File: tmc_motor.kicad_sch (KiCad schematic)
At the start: 10 parts

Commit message: starting layout
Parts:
- R202: renamed from R; footprint Resistor_SMD:R_0805_2012Metric_Pad1.20x1.40mm_HandSolder -> Resistor_SMD:R_0603_1608Metric_Pad0.98x0.95mm_HandSolder
- R203, R205: footprint Resistor_SMD:R_0805_2012Metric_Pad1.20x1.40mm_HandSolder -> Resistor_SMD:R_0603_1608Metric_Pad0.98x0.95mm_HandSolder
- SW201: renamed from SW; footprint (none) -> Button_Switch_THT:SW_DIP_SPSTx02_Slide_9.78x7.26mm_W7.62mm_P2.54mm
- renumbered C to C202, J to J201, U to U201

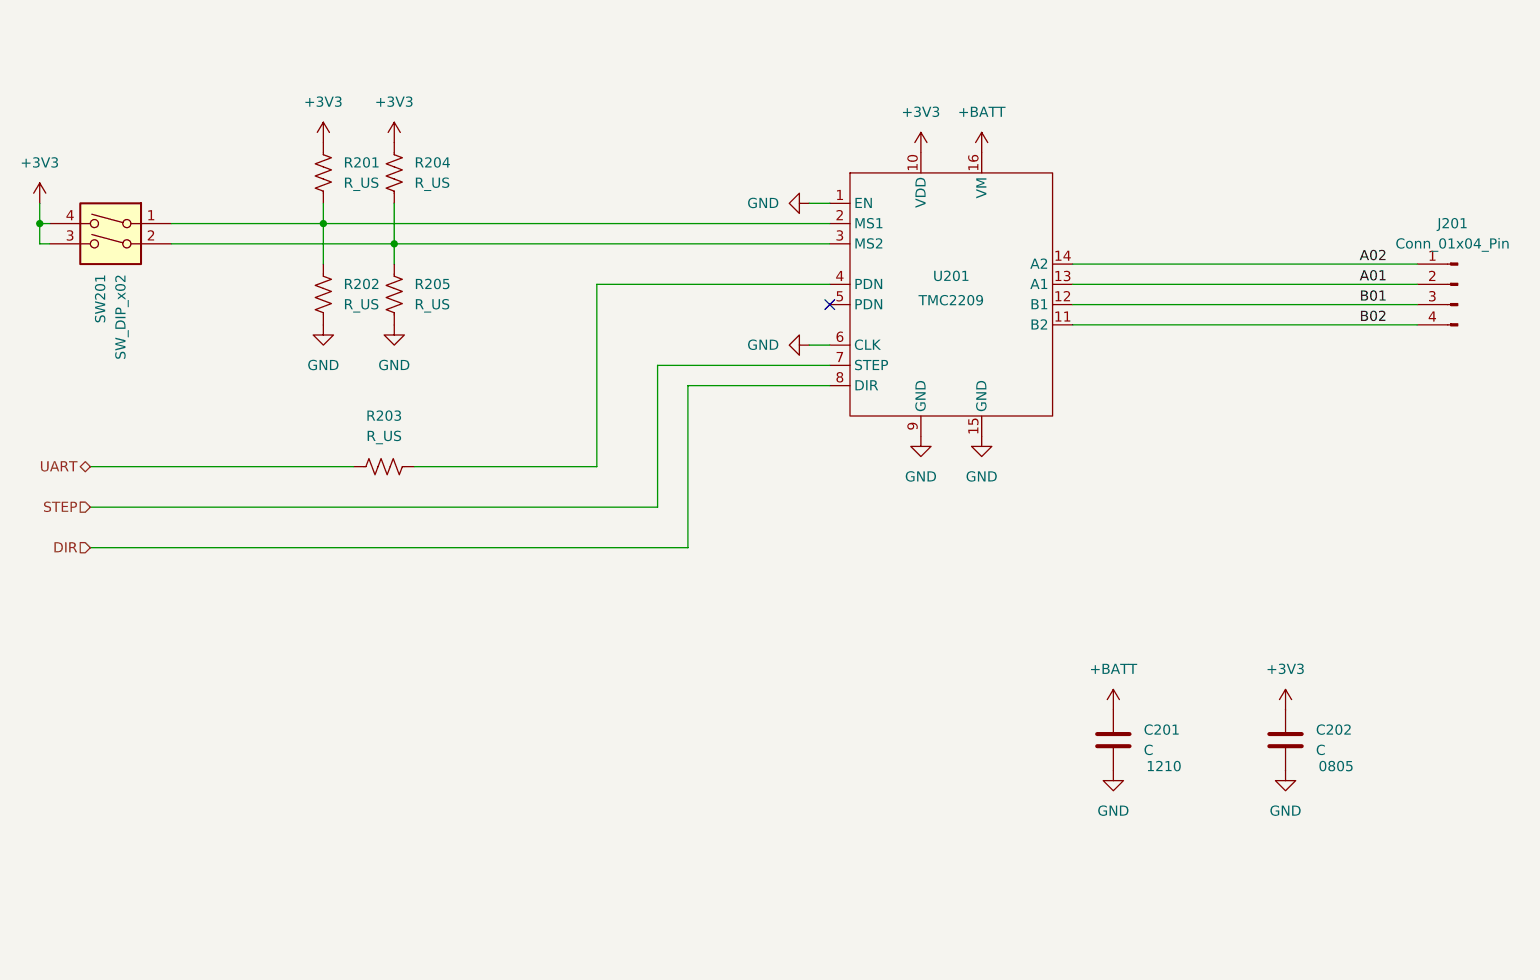
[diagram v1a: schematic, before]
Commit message: Add net class
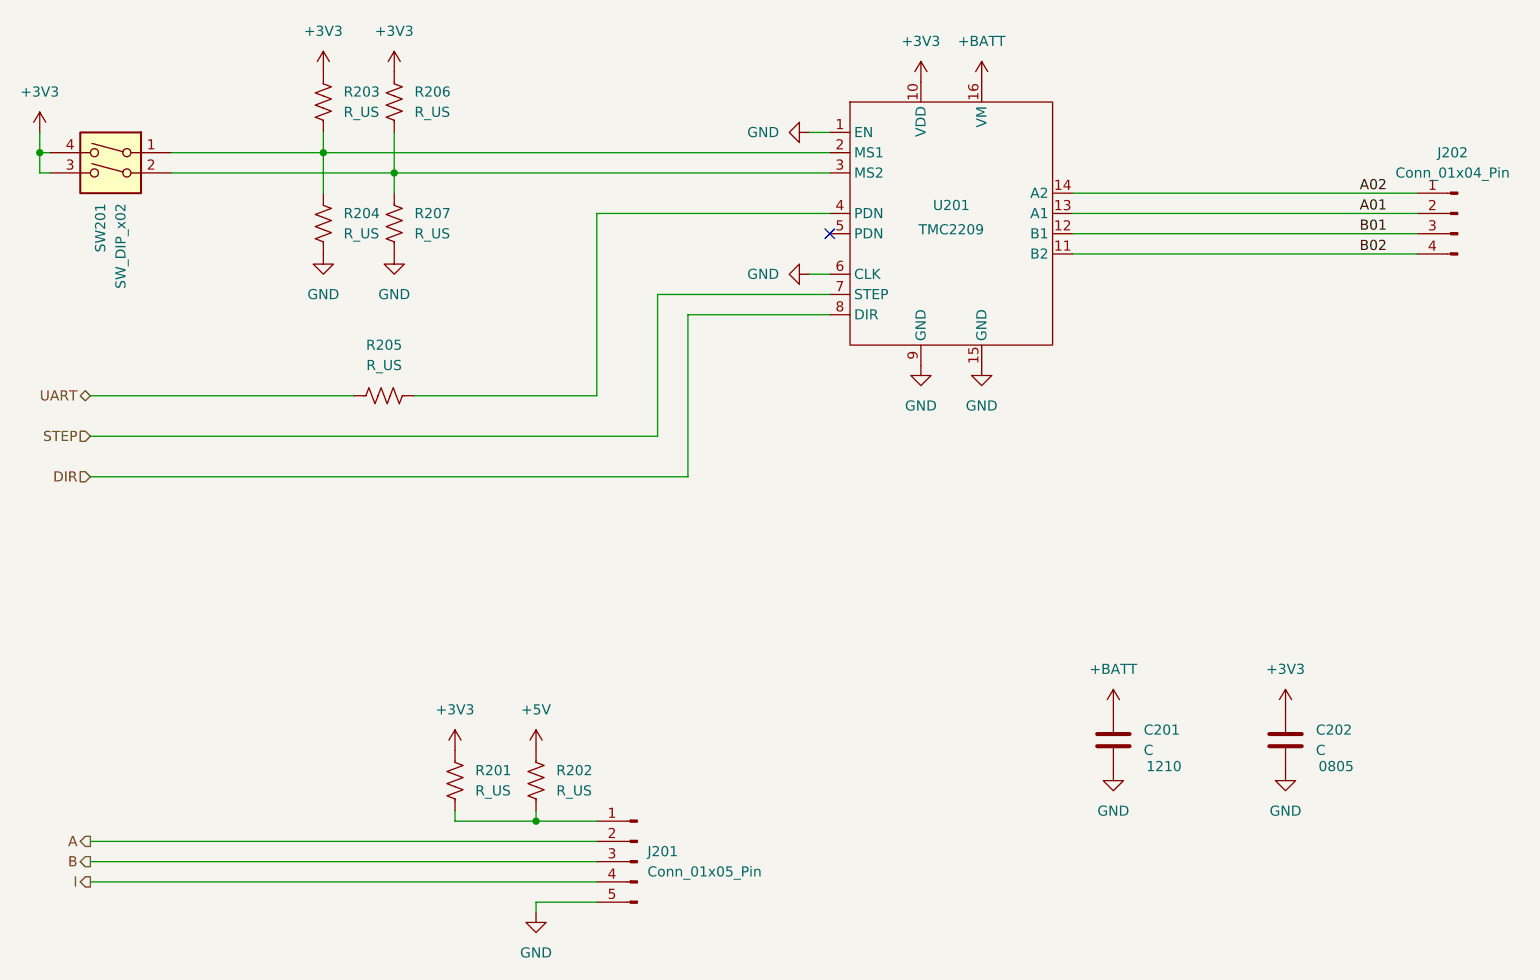
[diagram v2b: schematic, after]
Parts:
- added J201: Conn_01x05_Pin, Connector_Molex:Molex_KK-254_AE-6410-05A_1x05_P2.54mm_Vertical, symbol Connector:Conn_01x05_Pin
- added R201, R202: R_US, Resistor_SMD:R_0603_1608Metric_Pad0.98x0.95mm_HandSolder, symbol Device:R_US
- renumbered J201 to J202, R201 to R203, R202 to R204, R203 to R205, R204 to R206, R205 to R207
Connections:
- net +3V3: now also R201.2
- net GND: now also J201.5 (Pin_5)
- new net: J201.1 (Pin_1), R201.1, R202.1
- new net +5V: R202.2
- new net A: J201.2 (Pin_2)
- new net B: J201.3 (Pin_3)
- new net I: J201.4 (Pin_4)
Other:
- moved on the sheet: J202, R203, R204, R205, R206, R207, SW201, U201

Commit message: move encoder pull up resistor to tmc sheet
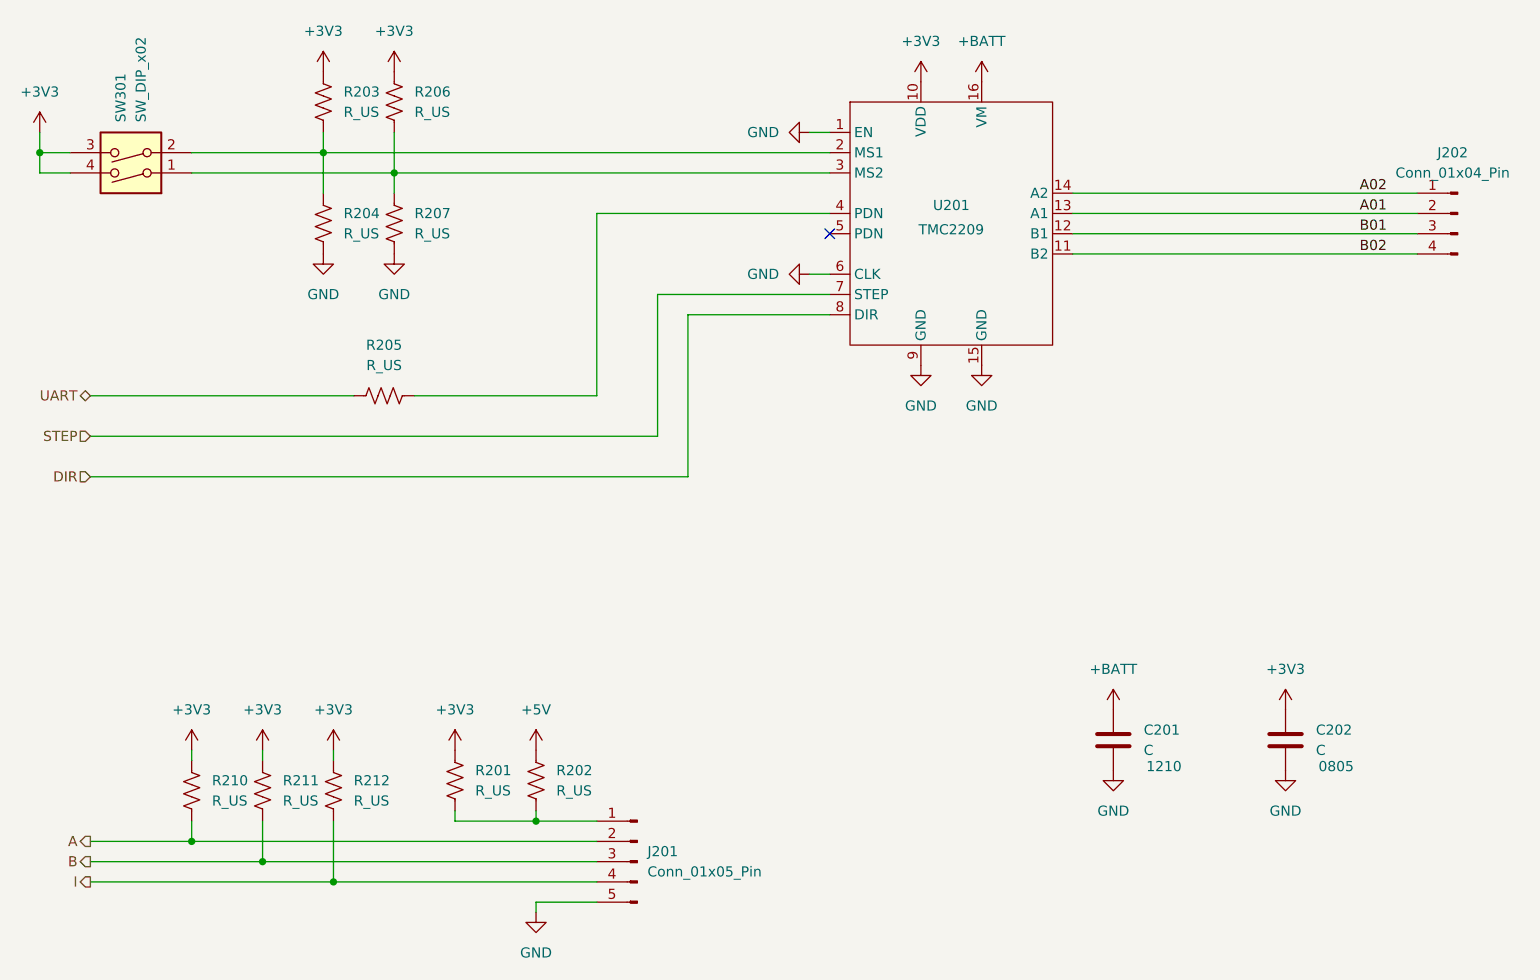
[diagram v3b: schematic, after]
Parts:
- added R210, R211, R212: R_US, Resistor_SMD:R_0603_1608Metric_Pad0.98x0.95mm_HandSolder, symbol Device:R_US
- renumbered SW201 to SW301
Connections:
- net +3V3: now also R210.2, R211.2, R212.2
- net A: now also R210.1
- net B: now also R211.1
- net I: now also R212.1
- net at R206.2, R207.1, U201.3 (MS2): now also SW301.1; no longer SW301.2
- net at R203.2, R204.1, U201.2 (MS1): now also SW301.2; no longer SW301.1
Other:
- moved on the sheet: SW301

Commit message: hrtim
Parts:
- removed R205: R_US, Resistor_SMD:R_0603_1608Metric_Pad0.98x0.95mm_HandSolder, symbol Device:R_US
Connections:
- net UART: now also U201.4 (PDN)
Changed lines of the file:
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@@
 	(wire
 		(pts
-			(xy 57.15 102.87) (xy 90.17 102.87)
+			(xy 57.15 102.87) (xy 120.65 102.87)
 		)
 		(stroke
@@
 		(pts
 			(xy 69.85 158.75) (xy 120.65 158.75)
-		)
-		(stroke
-			(width 0)
-			(type default)
-		)
-	)
-	(wire
-		(pts
-			(xy 97.79 102.87) (xy 120.65 102.87)
 		)
 		(stroke
@@
 					(unit 1)
 				)
-			)
-		)
-	)
-	(symbol
-		(lib_id "Device:R_US")
-		(at 93.98 102.87 90)
-		(unit 1)
-		(exclude_from_sim no)
-		(in_bom yes)
-		(on_board yes)
-		(dnp no)
-		(fields_autoplaced yes)
-		(property "Reference" "R205"
-			(at 93.98 96.52 90)
-			(effects
-				(font
-					(size 1.27 1.27)
-				)
-			)
-		)
-		(property "Value" "R_US"
-			(at 93.98 99.06 90)
-			(effects
-				(font
-					(size 1.27 1.27)
-				)
-			)
-		)
-		(property "Footprint" "Resistor_SMD:R_0603_1608Metric_Pad0.98x0.95mm_HandSolder"
-			(at 94.234 101.854 90)
-			(effects
-				(font
-					(size 1.27 1.27)
-				)
-				(hide yes)
-			)
-		)
-		(property "Datasheet" "~"
-			(at 93.98 102.87 0)
-			(effects
-				(font
-					(size 1.27 1.27)
-				)
-				(hide yes)
-			)
-		)
-		(property "Description" "Resistor, US symbol"
-			(at 93.98 102.87 0)
-			(effects
-				(font
-					(size 1.27 1.27)
-				)
-				(hide yes)
-			)
-		)
-		(pin "1"
-		)
-		(pin "2"
-		)
-		(instances
-			(project "Carte_moteur"
-				(path "/5d858058-eb89-4613-a7ba-0652b9f0936c/3601c837-7861-4e39-9e5f-37bf5bd7778d"
-					(reference "R205")
-					(unit 1)
-				)
-				(path "/5d858058-eb89-4613-a7ba-0652b9f0936c/37d501de-32d1-405a-b67e-90954dd4eb6d"
-					(reference "R405")
-					(unit 1)
-				)
-				(path "/5d858058-eb89-4613-a7ba-0652b9f0936c/775cd45e-9174-4367-b4d9-b516ea5d1b35"
-					(reference "R305")
-					(unit 1)
-				)

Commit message: before trying new µC orientation
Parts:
- removed SW301: SW_DIP_x02, Button_Switch_THT:SW_DIP_SPSTx02_Slide_9.78x7.26mm_W7.62mm_P2.54mm, symbol Switch:SW_DIP_x02
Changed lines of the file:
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@@
 	(paper "A4")
-	(junction
-		(at 50.8 72.39)
-		(diameter 0)
-		(color 0 0 0 0)
-	)
 	(junction
 		(at 78.74 161.29)
@@
 	(wire
 		(pts
-			(xy 50.8 74.93) (xy 54.61 74.93)
-		)
-		(stroke
-			(width 0)
-			(type default)
-		)
-	)
-	(wire
-		(pts
 			(xy 102.87 156.21) (xy 113.03 156.21)
 		)
@@
 	(wire
 		(pts
-			(xy 69.85 74.93) (xy 95.25 74.93)
-		)
-		(stroke
-			(width 0)
-			(type default)
-		)
-	)
-	(wire
-		(pts
 			(xy 87.63 163.83) (xy 120.65 163.83)
 		)
@@
 	(wire
 		(pts
-			(xy 69.85 72.39) (xy 86.36 72.39)
-		)
-		(stroke
-			(width 0)
-			(type default)
-		)
-	)
-	(wire
-		(pts
 			(xy 128.27 90.17) (xy 128.27 107.95)
 		)
@@
 	(wire
 		(pts
-			(xy 50.8 72.39) (xy 50.8 69.85)
-		)
-		(stroke
-			(width 0)
-			(type default)
-		)
-	)
-	(wire
-		(pts
 			(xy 57.15 113.03) (xy 132.08 113.03)
 		)
@@
 	(wire
 		(pts
-			(xy 54.61 72.39) (xy 50.8 72.39)
-		)
-		(stroke
-			(width 0)
-			(type default)
-		)
-	)
-	(wire
-		(pts
 			(xy 78.74 161.29) (xy 120.65 161.29)
 		)
@@
 		(pts
 			(xy 120.65 80.01) (xy 149.86 80.01)
-		)
-		(stroke
-			(width 0)
-			(type default)
-		)
-	)
-	(wire
-		(pts
-			(xy 50.8 72.39) (xy 50.8 74.93)
 		)
 		(stroke
@@
 	)
 	(symbol
-		(lib_id "power:+3V3")
-		(at 50.8 69.85 0)
-		(unit 1)
-		(exclude_from_sim no)
-		(in_bom yes)
-		(on_board yes)
-		(dnp no)
-		(fields_autoplaced yes)
-		(property "Reference" "#PWR0201"
-			(at 50.8 73.66 0)
-			(effects
-				(font
-					(size 1.27 1.27)
-				)
-				(hide yes)
-			)
-		)
-		(property "Value" "+3V3"
-			(at 50.8 64.77 0)
-			(effects
-				(font
-					(size 1.27 1.27)
-				)
-			)
-		)
-		(property "Footprint" ""
-			(at 50.8 69.85 0)
-			(effects
-				(font
-					(size 1.27 1.27)
-				)
-				(hide yes)
-			)
-		)
-		(property "Datasheet" ""
-			(at 50.8 69.85 0)
-			(effects
-				(font
-					(size 1.27 1.27)
-				)
-				(hide yes)
-			)
-		)
-		(property "Description" "Power symbol creates a global label with name \"+3V3\""
-			(at 50.8 69.85 0)
-			(effects
-				(font
-					(size 1.27 1.27)
-				)
-				(hide yes)
-			)
-		)
-		(pin "1"
-		)
-		(instances
-			(project "Carte_moteur"
-				(path "/5d858058-eb89-4613-a7ba-0652b9f0936c/3601c837-7861-4e39-9e5f-37bf5bd7778d"
-					(reference "#PWR0201")
-					(unit 1)
-				)
-				(path "/5d858058-eb89-4613-a7ba-0652b9f0936c/37d501de-32d1-405a-b67e-90954dd4eb6d"
-					(reference "#PWR0401")
-					(unit 1)
-				)
-				(path "/5d858058-eb89-4613-a7ba-0652b9f0936c/775cd45e-9174-4367-b4d9-b516ea5d1b35"
-					(reference "#PWR0301")
-					(unit 1)
-				)
-			)
-		)
-	)
-	(symbol
 		(lib_id "power:GND")
 		(at 168.91 99.06 0)
@@
 					(unit 1)
 				)
-			)
-		)
-	)
-	(symbol
-		(lib_id "Switch:SW_DIP_x02")
-		(at 62.23 72.39 180)
-		(unit 1)
-		(exclude_from_sim no)
-		(in_bom yes)
-		(on_board yes)
-		(dnp no)
-		(property "Reference" "SW301"
-			(at 60.9599 68.58 90)
-			(effects
-				(font
-					(size 1.27 1.27)
-				)
-				(justify right)
-			)
-		)
-		(property "Value" "SW_DIP_x02"
-			(at 63.4999 68.58 90)
-			(effects
-				(font
-					(size 1.27 1.27)
-				)
-				(justify right)
-			)
-		)
-		(property "Footprint" "Button_Switch_THT:SW_DIP_SPSTx02_Slide_9.78x7.26mm_W7.62mm_P2.54mm"
-			(at 62.23 72.39 0)
-			(effects
-				(font
-					(size 1.27 1.27)
-				)
-				(hide yes)
-			)
-		)
-		(property "Datasheet" "~"
-			(at 62.23 72.39 0)
-			(effects
-				(font
-					(size 1.27 1.27)
-				)
-				(hide yes)
-			)
-		)
-		(property "Description" "2x DIP Switch, Single Pole Single Throw (SPST) switch, small symbol"
-			(at 62.23 72.39 0)
-			(effects
-				(font
-					(size 1.27 1.27)
-				)
-				(hide yes)
-			)
-		)
-		(pin "1"
-		)
-		(pin "2"
-		)
-		(pin "4"
-		)
-		(pin "3"
-		)
-		(instances
-			(project "Carte_moteur"
-				(path "/5d858058-eb89-4613-a7ba-0652b9f0936c/3601c837-7861-4e39-9e5f-37bf5bd7778d"
-					(reference "SW301")
-					(unit 1)
-				)
-				(path "/5d858058-eb89-4613-a7ba-0652b9f0936c/37d501de-32d1-405a-b67e-90954dd4eb6d"
-					(reference "SW303")
-					(unit 1)
-				)
-				(path "/5d858058-eb89-4613-a7ba-0652b9f0936c/775cd45e-9174-4367-b4d9-b516ea5d1b35"
-					(reference "SW302")
-					(unit 1)
-				)
